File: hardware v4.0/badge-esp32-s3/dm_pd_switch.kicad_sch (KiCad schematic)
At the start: 2 parts, among them SW2 TS-1088-AR02016

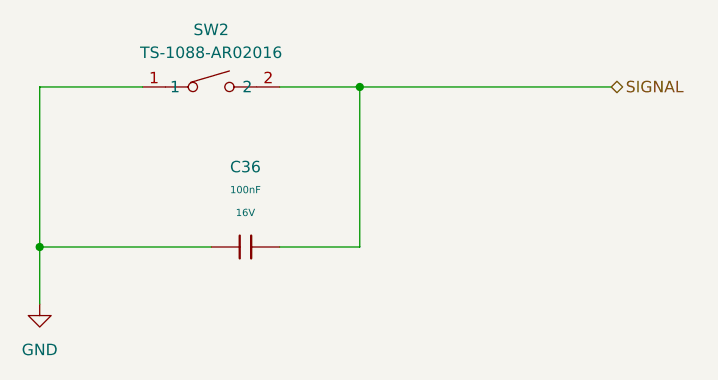
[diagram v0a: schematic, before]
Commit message: added 470R resistor to boot switch to prevent conflict
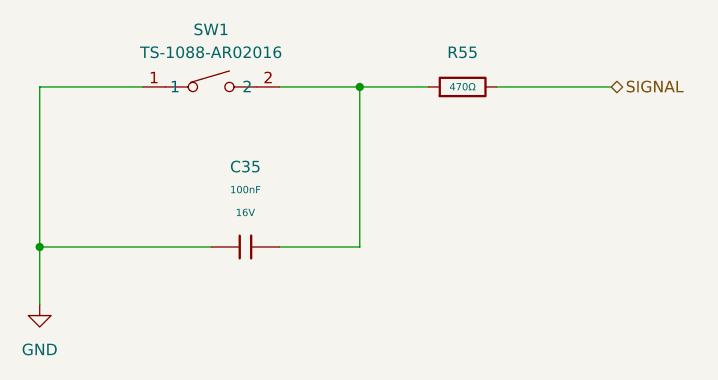
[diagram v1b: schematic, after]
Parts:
- added R55: 470Ω, PCM_JLCPCB:R_0402, symbol PCM_JLCPCB-Resistors:0402,470Ω
- renumbered C36 to C35, SW2 to SW1
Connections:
- net SIGNAL: now also R55.2; no longer C35.2, SW1.2
- new net: C35.2, R55.1, SW1.2
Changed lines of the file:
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@@
+	(wire
+		(pts
+			(xy 184.15 86.36) (xy 171.45 86.36)
+		)
+		(stroke
+			(width 0)
+			(type default)
+		)
+	)
 	(wire
 		(pts
@@
 	(wire
 		(pts
-			(xy 156.21 86.36) (xy 184.15 86.36)
+			(xy 163.83 86.36) (xy 156.21 86.36)
 		)
 		(stroke
@@
 			)
 			(justify left)
+		)
+	)
+	(symbol
+		(lib_id "PCM_JLCPCB-Resistors:0402,470Ω")
+		(at 167.64 86.36 90)
+		(unit 1)
+		(exclude_from_sim no)
+		(in_bom yes)
+		(on_board yes)
+		(dnp no)
+		(fields_autoplaced yes)
+		(property "Reference" "R55"
+			(at 167.64 82.55 90)
+			(effects
+				(font
+					(size 1.27 1.27)
+				)
+			)
+		)
+		(property "Value" "470Ω"
+			(at 167.64 86.36 90)
+			(do_not_autoplace yes)
+			(effects
+				(font
+					(size 0.8 0.8)
+				)
+			)
+		)
+		(property "Footprint" "PCM_JLCPCB:R_0402"
+			(at 167.64 88.138 90)
+			(effects
+				(font
+					(size 1.27 1.27)
+				)
+				(hide yes)
+			)
+		)
+		(property "Datasheet" "https://www.lcsc.com/datasheet/lcsc_datasheet_2205311900_UNI-ROYAL-Uniroyal-Elec-0402WGF4700TCE_C25117.pdf"
+			(at 167.64 86.36 0)
+			(effects
+				(font
+					(size 1.27 1.27)
+				)
+				(hide yes)
+			)
+		)
+		(property "Description" "62.5mW Thick Film Resistors 50V ±100ppm/°C ±1% 470Ω 0402 Chip Resistor - Surface Mount ROHS"
+			(at 167.64 86.36 0)
+			(effects
+				(font
+					(size 1.27 1.27)
+				)
+				(hide yes)
+			)
+		)
+		(property "LCSC" "C25117"
+			(at 167.64 86.36 0)
+			(effects
+				(font
+					(size 1.27 1.27)
+				)
+				(hide yes)
+			)
+		)
+		(property "Stock" "1007760"
+			(at 167.64 86.36 0)
+			(effects
+				(font
+					(size 1.27 1.27)
+				)
+				(hide yes)
+			)
+		)
+		(property "Price" "0.004USD"
+			(at 167.64 86.36 0)
+			(effects
+				(font
+					(size 1.27 1.27)
+				)
+				(hide yes)
+			)
+		)
+		(property "Process" "SMT"
+			(at 167.64 86.36 0)
+			(effects
+				(font
+					(size 1.27 1.27)
+				)
+				(hide yes)
+			)
+		)
+		(property "Minimum Qty" "20"
+			(at 167.64 86.36 0)
+			(effects
+				(font
+					(size 1.27 1.27)
+				)
+				(hide yes)
+			)
+		)
+		(property "Attrition Qty" "10"
+			(at 167.64 86.36 0)
+			(effects
+				(font
+					(size 1.27 1.27)
+				)
+				(hide yes)
+			)
+		)
+		(property "Class" "Basic Component"
+			(at 167.64 86.36 0)
+			(effects
+				(font
+					(size 1.27 1.27)
+				)
+				(hide yes)
+			)
+		)
+		(property "Category" "Resistors,Chip Resistor - Surface Mount"
+			(at 167.64 86.36 0)
+			(effects
+				(font
+					(size 1.27 1.27)
+				)
+				(hide yes)
+			)
+		)
+		(property "Manufacturer" "UNI-ROYAL(Uniroyal Elec)"
+			(at 167.64 86.36 0)
+			(effects
+				(font
+					(size 1.27 1.27)
+				)
+				(hide yes)
+			)
+		)
+		(property "Part" "0402WGF4700TCE"
+			(at 167.64 86.36 0)
+			(effects
+				(font
+					(size 1.27 1.27)
+				)
+				(hide yes)
+			)
+		)
+		(property "Resistance" "470Ω"
+			(at 167.64 86.36 0)
+			(effects
+				(font
+					(size 1.27 1.27)
+				)
+				(hide yes)
+			)
+		)
+		(property "Power(Watts)" "62.5mW"
+			(at 167.64 86.36 0)
+			(effects
+				(font
+					(size 1.27 1.27)
+				)
+				(hide yes)
+			)
+		)
+		(property "Type" "Thick Film Resistors"
+			(at 167.64 86.36 0)
+			(effects
+				(font
+					(size 1.27 1.27)
+				)
+				(hide yes)
+			)
+		)
+		(property "Overload Voltage (Max)" "50V"
+			(at 167.64 86.36 0)
+			(effects
+				(font
+					(size 1.27 1.27)
+				)
+				(hide yes)
+			)
+		)
+		(property "Operating Temperature Range" "-55°C~+155°C"
+			(at 167.64 86.36 0)
+			(effects
+				(font
+					(size 1.27 1.27)
+				)
+				(hide yes)
+			)
+		)
+		(property "Tolerance" "±1%"
+			(at 167.64 86.36 0)
+			(effects
+				(font
+					(size 1.27 1.27)
+				)
+				(hide yes)
+			)
+		)
+		(property "Temperature Coefficient" "±100ppm/°C"
+			(at 167.64 86.36 0)
+			(effects
+				(font
+					(size 1.27 1.27)
+				)
+				(hide yes)
+			)
+		)
+		(pin "2"
+		)
+		(pin "1"
+		)
+		(instances
+			(project ""
+				(path "/e2af9a6c-dbe9-4de2-9ba6-ea213a7300ec/b79c388b-f340-4022-8bff-2018e70f780a"
+					(reference "R55")
+					(unit 1)
+				)
+			)
 		)
 	)
@@
 		(dnp no)
 		(fields_autoplaced yes)
-		(property "Reference" "SW2"
+		(property "Reference" "SW1"
 			(at 139.7 80.01 0)
 			(effects
@@
 		(dnp no)
 		(fields_autoplaced yes)
-		(property "Reference" "#PWR028"
+		(property "Reference" "#PWR027"
 			(at 120.65 116.84 0)
 			(effects
@@
 		(dnp no)
 		(fields_autoplaced yes)
-		(property "Reference" "C36"
+		(property "Reference" "C35"
 			(at 143.51 95.25 90)
 			(effects
